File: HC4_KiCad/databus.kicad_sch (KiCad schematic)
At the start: 11 parts, among them IC10 74HC4002, IC8 74HC257, IC9 74HC244, J3 Expantion_Connector

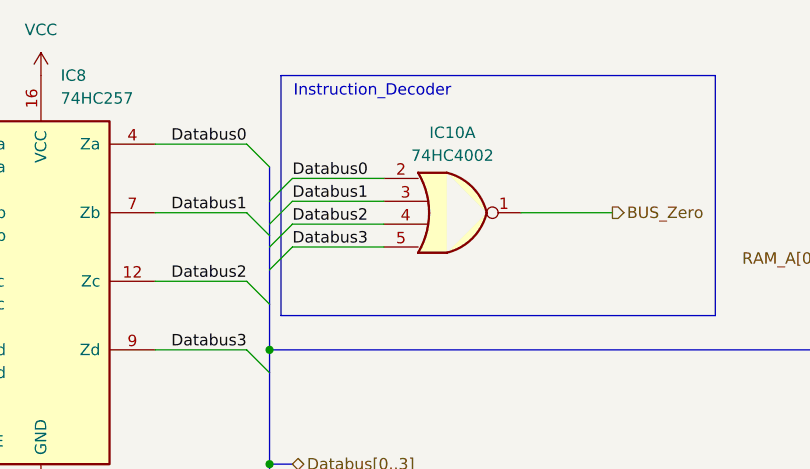
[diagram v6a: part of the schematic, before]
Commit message: とりあえずIC配置確定
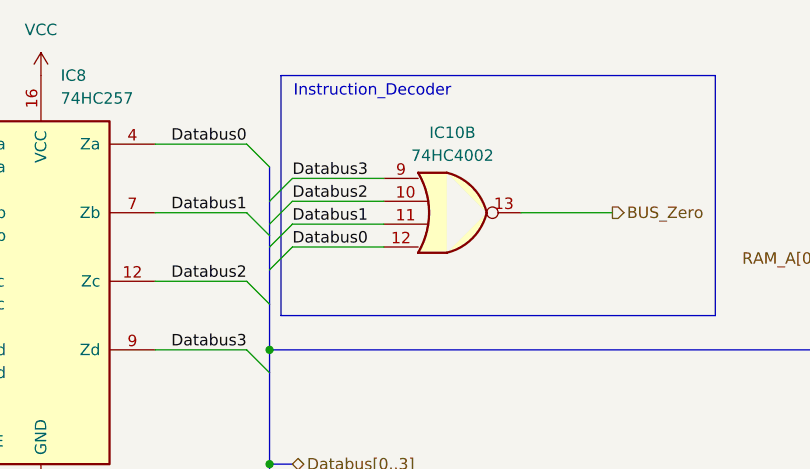
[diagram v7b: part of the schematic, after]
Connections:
- net BUS_Zero: now also IC10.13; no longer IC10.1
- net Databus0: now also IC10.12; no longer IC10.2
- net Databus1: now also IC10.11; no longer IC10.3
- net Databus2: now also IC10.10; no longer IC10.4
- net Databus3: now also IC10.9; no longer IC10.5
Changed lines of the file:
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@@
 	)
 	(label "Databus3"
-		(at 127 68.58 0)
+		(at 127 60.96 0)
 		(fields_autoplaced yes)
 		(effects
@@
 	)
 	(label "Databus1"
-		(at 127 63.5 0)
+		(at 127 66.04 0)
 		(fields_autoplaced yes)
 		(effects
@@
 	)
 	(label "Databus2"
-		(at 127 66.04 0)
+		(at 127 63.5 0)
 		(fields_autoplaced yes)
 		(effects
@@
 	)
 	(label "Databus0"
-		(at 127 60.96 0)
+		(at 127 68.58 0)
 		(fields_autoplaced yes)
 		(effects
@@
 		(lib_id "74xx_2:74HC4002")
 		(at 144.78 64.77 0)
-		(unit 1)
+		(unit 2)
 		(exclude_from_sim no)
 		(in_bom yes)
@@
 				(path "/33731ded-38c0-4297-bdd8-92b082f46ff8/294cbb59-ed60-4be2-81ec-3da02c446083"
 					(reference "IC10")
-					(unit 1)
-				)
-			)
+					(unit 2)
+				)
+			)

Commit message: またも手直し
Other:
- title: CPU -> HC4_CPU
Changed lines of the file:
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@@
 	(paper "A4")
 	(title_block
-		(title "CPU")
-		(date "2025-02-09")
-		(rev "1.0")
+		(title "HC4_CPU")
+		(date "2025-02-23")
+		(rev "1.2")
 	)
 	(junction
@@
 	(label "ALU0"
 		(at 81.28 57.15 0)
-		(fields_autoplaced yes)
 		(effects
 			(font
@@
 	(label "Databus1"
 		(at 121.92 123.19 180)
-		(fields_autoplaced yes)
 		(effects
 			(font
@@
 	(label "Stack0"
 		(at 137.16 106.68 0)
-		(fields_autoplaced yes)
 		(effects
 			(font
@@
 	(label "Databus1"
 		(at 76.2 133.35 0)
-		(fields_autoplaced yes)
 		(effects
 			(font
@@
 	(label "Level_C0"
 		(at 77.47 59.69 0)
-		(fields_autoplaced yes)
 		(effects
 			(font
@@
 	(label "Stack2"
 		(at 137.16 101.6 0)
-		(fields_autoplaced yes)
 		(effects
 			(font
@@
 	(label "Databus3"
 		(at 127 99.06 0)
-		(fields_autoplaced yes)
 		(effects
 			(font
@@
 	(label "Databus3"
 		(at 127 60.96 0)
-		(fields_autoplaced yes)
 		(effects
 			(font
@@
 	(label "Databus1"
 		(at 127 66.04 0)
-		(fields_autoplaced yes)
 		(effects
 			(font
@@
 	(label "Databus0"
 		(at 76.2 130.81 0)
-		(fields_autoplaced yes)
 		(effects
 			(font
@@
 	(label "Databus2"
 		(at 121.92 72.39 180)
-		(fields_autoplaced yes)
 		(effects
 			(font
@@
 	(label "Databus3"
 		(at 121.92 128.27 180)
-		(fields_autoplaced yes)
 		(effects
 			(font
@@
 	(label "Databus3"
 		(at 76.2 138.43 0)
-		(fields_autoplaced yes)
 		(effects
 			(font
@@
 	(label "Stack1"
 		(at 137.16 104.14 0)
-		(fields_autoplaced yes)
 		(effects
 			(font
@@
 	(label "Stack3"
 		(at 137.16 99.06 0)
-		(fields_autoplaced yes)
 		(effects
 			(font
@@
 	(label "Databus3"
 		(at 121.92 80.01 180)
-		(fields_autoplaced yes)
 		(effects
 			(font
@@
 	(label "Databus0"
 		(at 127 106.68 0)
-		(fields_autoplaced yes)
 		(effects
 			(font
@@
 	(label "Instruction_3"
 		(at 86.36 128.27 180)
-		(fields_autoplaced yes)
 		(effects
 			(font
@@
 	(label "RAM_A1"
 		(at 224.79 91.44 180)
-		(fields_autoplaced yes)
 		(effects
 			(font
@@
 	(label "RAM_A2"
 		(at 194.31 93.98 0)
-		(fields_autoplaced yes)
 		(effects
 			(font
@@
 	(label "ALU1"
 		(at 81.28 64.77 0)
-		(fields_autoplaced yes)
 		(effects
 			(font
@@
 	(label "RAM_A4"
 		(at 194.31 96.52 0)
-		(fields_autoplaced yes)
 		(effects
 			(font
@@
 	(label "Level_C2"
 		(at 77.47 74.93 0)
-		(fields_autoplaced yes)
 		(effects
 			(font
@@
 	(label "RAM_A5"
 		(at 224.79 96.52 180)
-		(fields_autoplaced yes)
 		(effects
 			(font
@@
 	(label "ALU2"
 		(at 81.28 72.39 0)
-		(fields_autoplaced yes)
 		(effects
 			(font
@@
 	(label "Databus1"
 		(at 121.92 64.77 180)
-		(fields_autoplaced yes)
 		(effects
 			(font
@@
 	(label "RAM_A6"
 		(at 194.31 99.06 0)
-		(fields_autoplaced yes)
 		(effects
 			(font
@@
 	(label "RAM_A7"
 		(at 224.79 99.06 180)
-		(fields_autoplaced yes)
 		(effects
 			(font
@@
 	(label "Level_C1"
 		(at 77.47 67.31 0)
-		(fields_autoplaced yes)
 		(effects
 			(font
@@
 	(label "Instruction_1"
 		(at 86.36 123.19 180)
-		(fields_autoplaced yes)
 		(effects
 			(font
@@
 	(label "Databus2"
 		(at 127 63.5 0)
-		(fields_autoplaced yes)
 		(effects
 			(font
@@
 	(label "Databus3"
 		(at 226.06 83.82 180)
-		(fields_autoplaced yes)
 		(effects
 			(font
@@
 	(label "Databus0"
 		(at 121.92 57.15 180)
-		(fields_autoplaced yes)
 		(effects
 			(font
@@
 	(label "RAM_A0"
 		(at 194.31 91.44 0)
-		(fields_autoplaced yes)
 		(effects
 			(font
@@
 	(label "Databus0"
 		(at 127 68.58 0)
-		(fields_autoplaced yes)
 		(effects
 			(font
@@
 	(label "Databus0"
 		(at 121.92 120.65 180)
-		(fields_autoplaced yes)
 		(effects
 			(font
@@
 	(label "Databus0"
 		(at 194.31 81.28 0)
-		(fields_autoplaced yes)
 		(effects
 			(font
@@
 	(label "Databus2"
 		(at 194.31 83.82 0)
-		(fields_autoplaced yes)
 		(effects
 			(font
@@
 	(label "Databus1"
 		(at 226.06 81.28 180)
-		(fields_autoplaced yes)
 		(effects
 			(font
@@
 	(label "Databus2"
 		(at 76.2 135.89 0)
-		(fields_autoplaced yes)
 		(effects
 			(font
@@
 	(label "Databus2"
 		(at 127 101.6 0)
-		(fields_autoplaced yes)
 		(effects
 			(font
@@
 	(label "Instruction_2"
 		(at 86.36 125.73 180)
-		(fields_autoplaced yes)
 		(effects
 			(font
@@
 	(label "Level_C3"
 		(at 77.47 82.55 0)
-		(fields_autoplaced yes)
 		(effects
 			(font
@@
 	(label "Instruction_0"
 		(at 86.36 120.65 180)
-		(fields_autoplaced yes)
 		(effects
 			(font
@@
 	(label "Databus2"
 		(at 121.92 125.73 180)
-		(fields_autoplaced yes)
 		(effects
 			(font
@@
 	(label "Databus1"
 		(at 127 104.14 0)
-		(fields_autoplaced yes)
 		(effects
 			(font
@@
 	(label "RAM_A3"
 		(at 224.79 93.98 180)
-		(fields_autoplaced yes)
 		(effects
 			(font
@@
 	(label "ALU3"
 		(at 81.28 80.01 0)
-		(fields_autoplaced yes)
 		(effects
 			(font
@@
 		(shape input)
 		(at 86.36 143.51 180)
-		(fields_autoplaced yes)
 		(effects
 			(font
@@
 		(shape output)
 		(at 147.32 99.06 0)
-		(fields_autoplaced yes)
 		(effects
 			(font
@@
 		(shape input)
 		(at 189.23 69.85 180)
-		(fields_autoplaced yes)
 		(effects
 			(font
@@
 		(shape input)
 		(at 86.36 87.63 180)
-		(fields_autoplaced yes)
 		(effects
 			(font
@@
 		(shape input)
 		(at 67.31 115.57 180)
-		(fields_autoplaced yes)
 		(effects
 			(font
@@
 		(shape input)
 		(at 72.39 57.15 180)
-		(fields_autoplaced yes)
 		(effects
 			(font
@@
 		(shape bidirectional)
 		(at 127 92.71 0)
-		(fields_autoplaced yes)
 		(effects
 			(font
@@
 		(shape input)
 		(at 215.9 78.74 0)
-		(fields_autoplaced yes)
 		(effects
 			(font
@@
 		(shape output)
 		(at 162.56 64.77 0)
-		(fields_autoplaced yes)
 		(effects
 			(font
@@
 		(shape input)
 		(at 86.36 90.17 180)
-		(fields_autoplaced yes)
 		(effects
 			(font
@@
 		(shape input)
 		(at 72.39 54.61 180)
-		(fields_autoplaced yes)
 		(effects
 			(font
@@
 		(shape input)
 		(at 203.2 78.74 180)
-		(fields_autoplaced yes)
-		(effects
-			(font
+		(effects
+			(font
